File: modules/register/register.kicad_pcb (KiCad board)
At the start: 2 copper layers, 113 x 103.5 mm, 30 parts, among them K0 4PDT, K1 4PDT, K2 4PDT, K3 4PDT

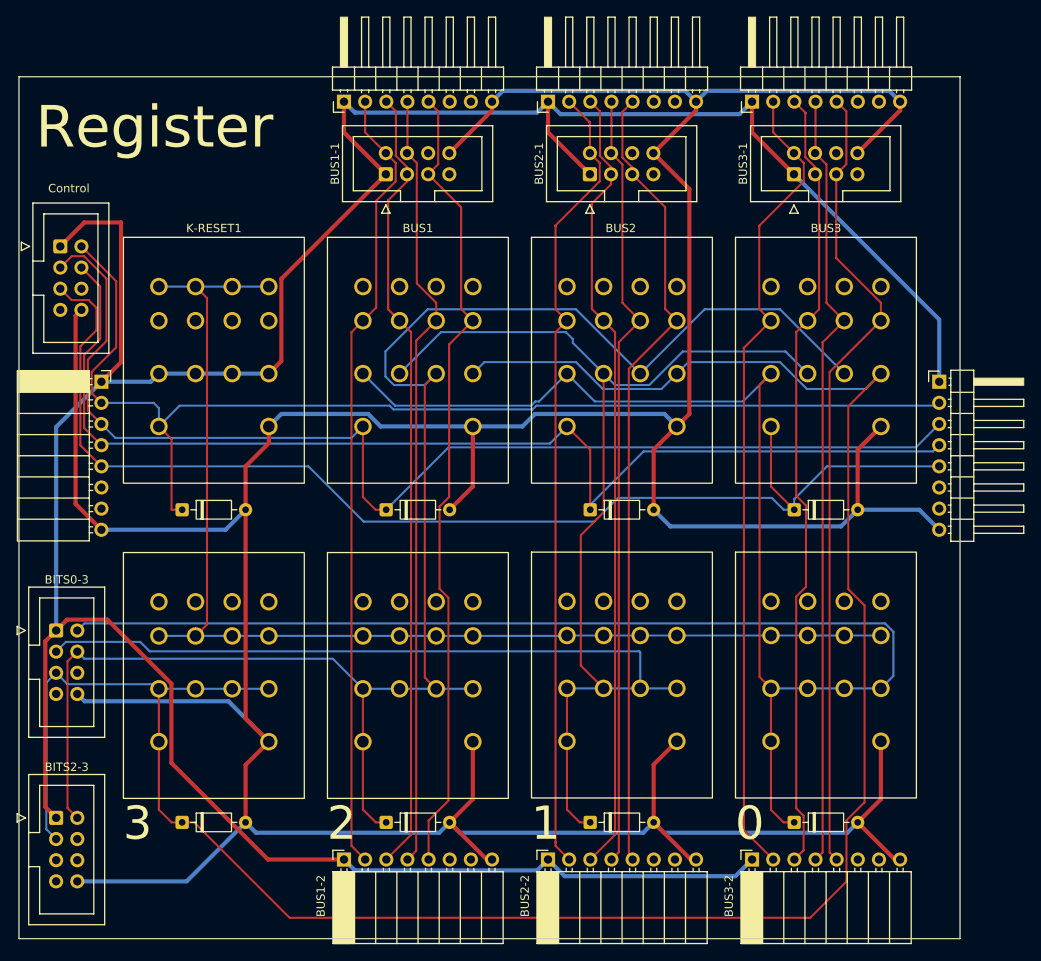
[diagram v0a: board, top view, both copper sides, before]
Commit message: Added some modules
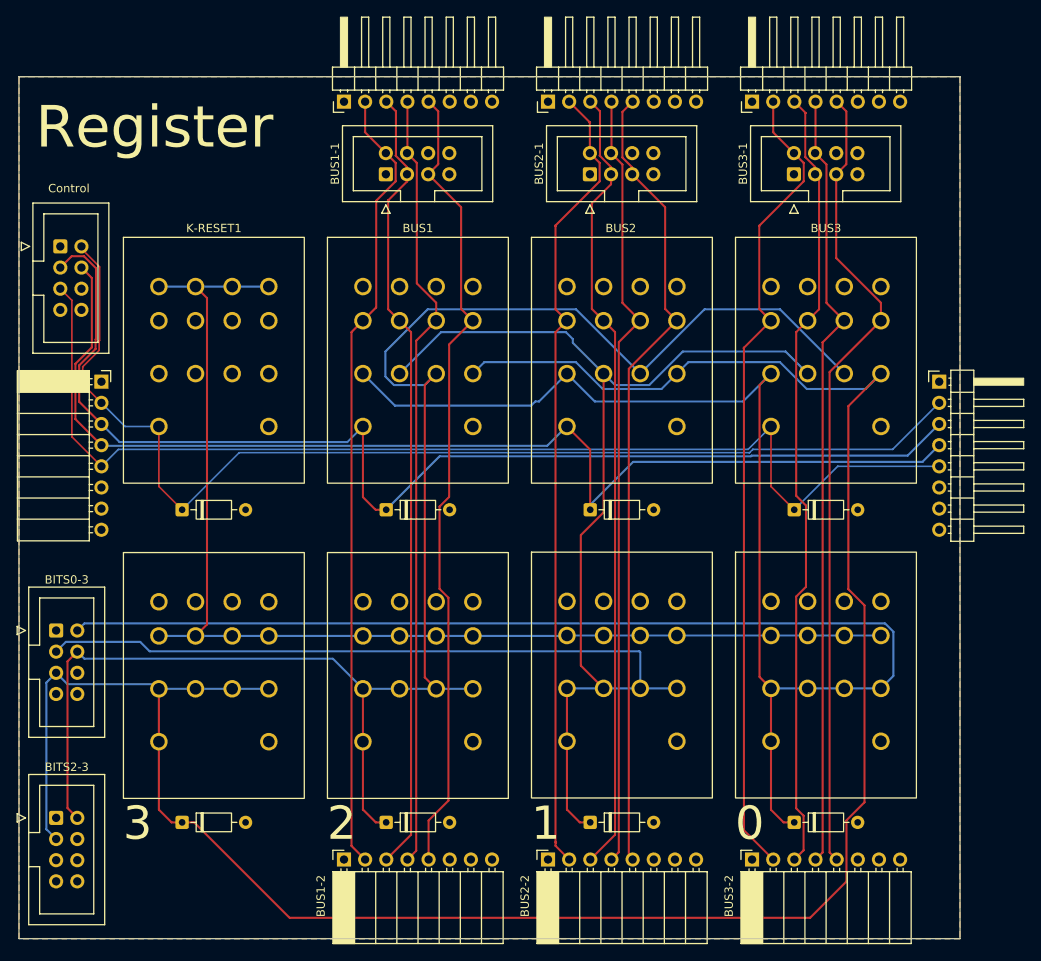
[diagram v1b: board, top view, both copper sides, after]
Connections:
- net Net-(BITS0-3-+V) renamed +24V
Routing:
- net GND: track 509.1 -> 0.00 mm
- net +24V: track 354.7 -> 0.00 mm
- net Net-(D8-K): track 145.3 -> 136.5 mm
- net Net-(D1-K): track 138.7 -> 136.3 mm
- net Net-(D7-K): track 137.4 -> 136.7 mm
- added copper zone on F.Cu, net +24V
- added copper zone on B.Cu, net GND
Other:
- board text added: "Register board rev6 P. Dovgalyuk, 2026"
- board text removed: "Register board rev5 P. Dovgalyuk, 2026"
